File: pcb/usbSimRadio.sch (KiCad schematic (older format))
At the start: 12 parts

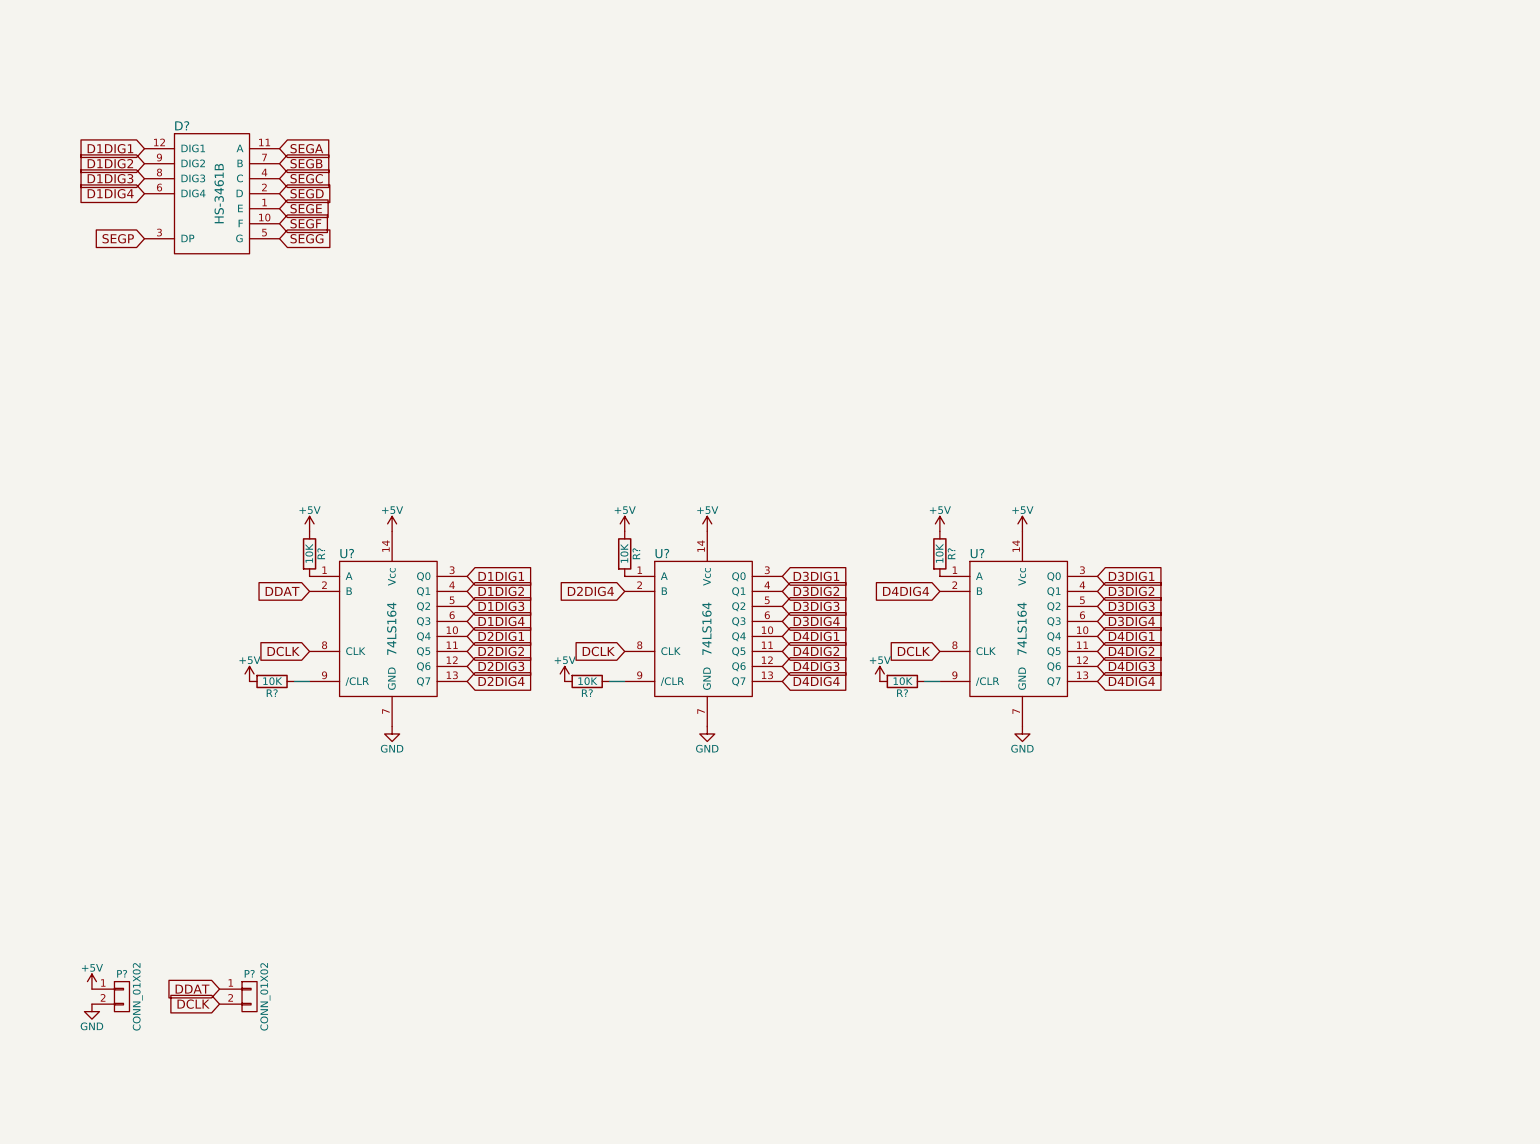
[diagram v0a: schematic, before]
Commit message: finished schematic and started on pcb
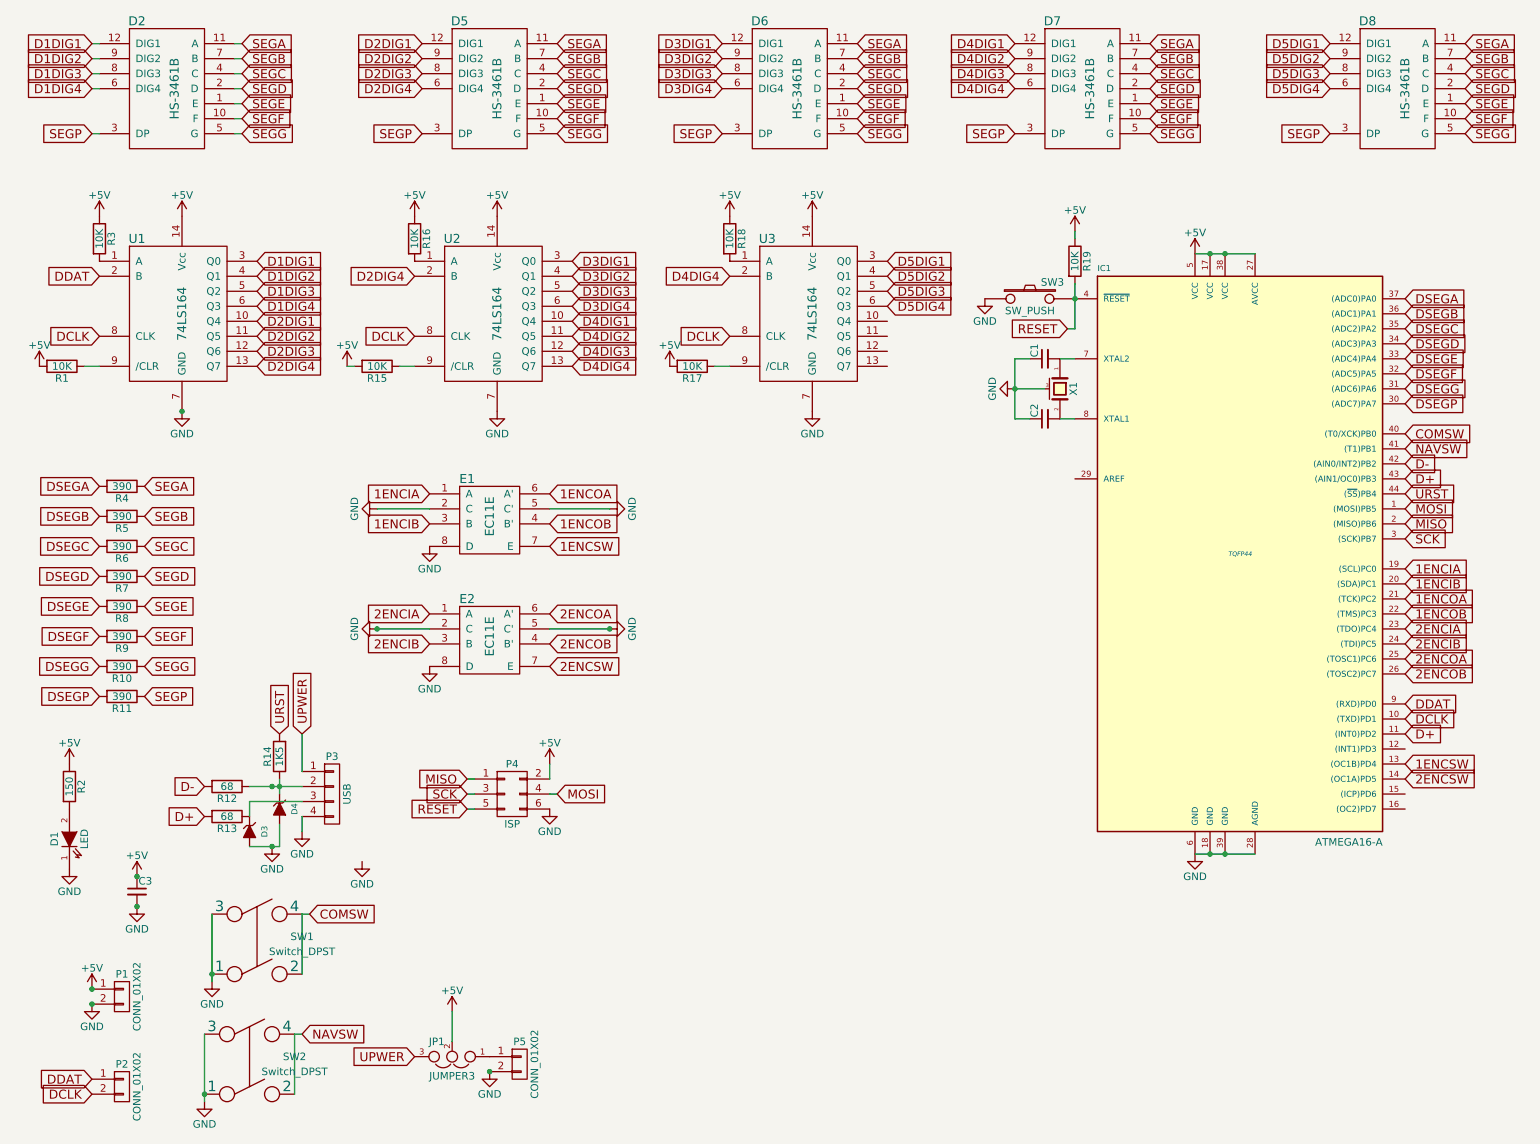
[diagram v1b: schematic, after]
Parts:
- added C1, C2, C3: C_Small, symbol C_Small
- added D1: LED, symbol LED
- added D3, D4: ZENERsmall, symbol ZENERsmall
- added D5, D6, D7, D8: HS-3461B, symbol HS-3461B
- added E1, E2: EC11E, symbol EC11E
- added IC1: ATMEGA16-A, TQFP44, symbol ATMEGA16-A
- added JP1: JUMPER3, symbol JUMPER3
- added P3: USB, symbol CONN_01X04
- added P4: ISP, symbol CONN_02X03
- added P5: CONN_01X02, symbol CONN_01X02
- added R10, R11, R4, R5, R6, R7, R8, R9: 390, symbol R
- added R12, R13: 68, symbol R
- added R14: 1K5, symbol R
- added R19: 10K, symbol R
- added R2: 150, symbol R
- added SW1, SW2: Switch_DPST, symbol Switch_DPST
- added SW3: SW_PUSH, symbol SW_PUSH
- added X1: CRYSTAL_SMD, symbol CRYSTAL_SMD
- gave numbers to parts that had none: 12
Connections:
- net +5V: now also C3.1, IC1.17 (VCC), IC1.27 (AVCC), IC1.38 (VCC), IC1.5 (VCC), JP1.2, P4.2 (P2), R19.1, R2.1
- net D2DIG1: now also D5.12 (DIG1)
- net D2DIG2: now also D5.9 (DIG2)
- net D2DIG3: now also D5.8 (DIG3)
- net D2DIG4: now also D5.6 (DIG4)
- net D3DIG1: now also D6.12 (DIG1); no longer U3.3 (Q0)
- net D3DIG2: now also D6.9 (DIG2); no longer U3.4 (Q1)
- net D3DIG3: now also D6.8 (DIG3); no longer U3.5 (Q2)
- net D3DIG4: now also D6.6 (DIG4); no longer U3.6 (Q3)
- net D4DIG1: now also D7.12 (DIG1); no longer U3.10 (Q4)
- net D4DIG2: now also D7.9 (DIG2); no longer U3.11 (Q5)
- net D4DIG3: now also D7.8 (DIG3); no longer U3.12 (Q6)
- net D4DIG4: now also D7.6 (DIG4); no longer U3.13 (Q7)
- net DCLK: now also IC1.10 ((TXD)PD1)
- net DDAT: now also IC1.9 ((RXD)PD0)
- net GND: now also C1.1, C2.1, C3.2, D1.1 (K), D3.2 (A), D4.2 (A), E1.2 (C), E1.5 (C'), E1.8 (D), E2.2 (C), E2.5 (C'), E2.8 (D), IC1.18 (GND), IC1.28 (AGND), IC1.39 (GND), IC1.6 (GND), P3.4 (P4), P4.6 (P6), P5.2 (P2), SW1.1, SW1.3, SW2.1, SW2.3, SW3.1, X1.3 (case)
- net SEGA: now also D5.11 (A), D6.11 (A), D7.11 (A), D8.11 (A), R4.1
- net SEGB: now also D5.7 (B), D6.7 (B), D7.7 (B), D8.7 (B), R5.1
- net SEGC: now also D5.4 (C), D6.4 (C), D7.4 (C), D8.4 (C), R6.1
- net SEGD: now also D5.2 (D), D6.2 (D), D7.2 (D), D8.2 (D), R7.1
- net SEGE: now also D5.1 (E), D6.1 (E), D7.1 (E), D8.1 (E), R8.1
- net SEGF: now also D5.10 (F), D6.10 (F), D7.10 (F), D8.10 (F), R9.1
- net SEGG: now also D5.5 (G), D6.5 (G), D7.5 (G), D8.5 (G), R10.1
- net SEGP: now also D5.3 (DP), D6.3 (DP), D7.3 (DP), D8.3 (DP), R11.1
- new net: C1.2, IC1.7 (XTAL2), X1.1
- new net: C2.2, IC1.8 (XTAL1), X1.2
- new net: JP1.1, P5.1 (P1)
- new net: D1.2 (A), R2.2
- new net: D4.1 (K), P3.2 (P2), R12.1, R14.1
- new net: D3.1 (K), P3.3 (P3), R13.1
- new net 1ENCIA: E1.1 (A), IC1.19 ((SCL)PC0)
- new net 1ENCIB: E1.3 (B), IC1.20 ((SDA)PC1)
- new net 1ENCOA: E1.6 (A'), IC1.21 ((TCK)PC2)
- new net 1ENCOB: E1.4 (B'), IC1.22 ((TMS)PC3)
- new net 1ENCSW: E1.7 (E), IC1.13 ((OC1B)PD4)
- new net 2ENCIA: E2.1 (A), IC1.23 ((TDO)PC4)
- new net 2ENCIB: E2.3 (B), IC1.24 ((TDI)PC5)
- new net 2ENCOA: E2.6 (A'), IC1.25 ((TOSC1)PC6)
- new net 2ENCOB: E2.4 (B'), IC1.26 ((TOSC2)PC7)
- new net 2ENCSW: E2.7 (E), IC1.14 ((OC1A)PD5)
- new net COMSW: IC1.40 ((T0/XCK)PB0), SW1.2, SW1.4
- new net D+: IC1.11 ((INT0)PD2), IC1.43 ((AIN1/OC0)PB3), R13.2
- new net D-: IC1.42 ((AIN0/INT2)PB2), R12.2
- new net D5DIG1: D8.12 (DIG1), U3.3 (Q0)
- new net D5DIG2: D8.9 (DIG2), U3.4 (Q1)
- new net D5DIG3: D8.8 (DIG3), U3.5 (Q2)
- new net D5DIG4: D8.6 (DIG4), U3.6 (Q3)
- new net DSEGA: IC1.37 ((ADC0)PA0), R4.2
- new net DSEGB: IC1.36 ((ADC1)PA1), R5.2
- new net DSEGC: IC1.35 ((ADC2)PA2), R6.2
- new net DSEGD: IC1.34 ((ADC3)PA3), R7.2
- new net DSEGE: IC1.33 ((ADC4)PA4), R8.2
- new net DSEGF: IC1.32 ((ADC5)PA5), R9.2
- new net DSEGG: IC1.31 ((ADC6)PA6), R10.2
- new net DSEGP: IC1.30 ((ADC7)PA7), R11.2
- new net MISO: IC1.2 ((MISO)PB6), P4.1 (P1)
- new net MOSI: IC1.1 ((MOSI)PB5), P4.4 (P4)
- new net NAVSW: IC1.41 ((T1)PB1), SW2.2, SW2.4
- new net RESET: IC1.4 (~RESET), P4.5 (P5), R19.2, SW3.2
- new net SCK: IC1.3 ((SCK)PB7), P4.3 (P3)
- new net UPWER: JP1.3, P3.1 (P1)
- new net URST: IC1.44 ((~SS~)PB4), R14.2
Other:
- moved on the sheet: D2, P2, R1, R15, R16, R17, R18, R3, U1, U2, U3
